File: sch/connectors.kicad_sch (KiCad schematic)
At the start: 79 parts, among them X1 Expansion, X4 PSU

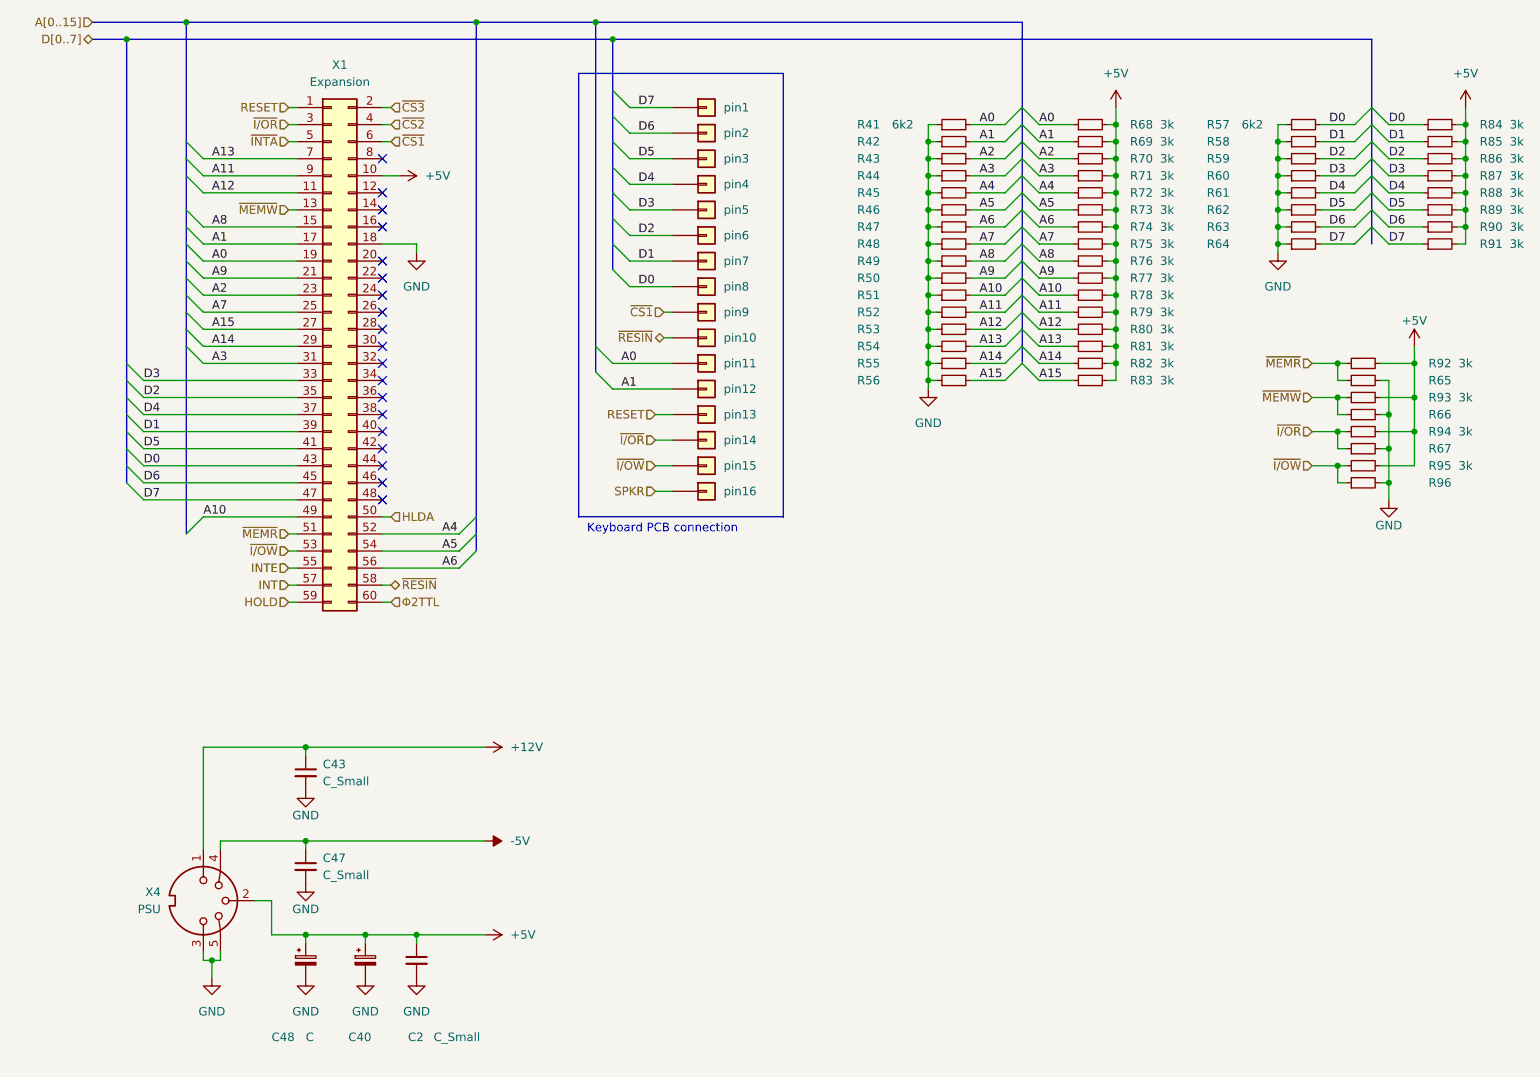
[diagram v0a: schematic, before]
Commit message: Schematics completed with values
Visual corrections pending
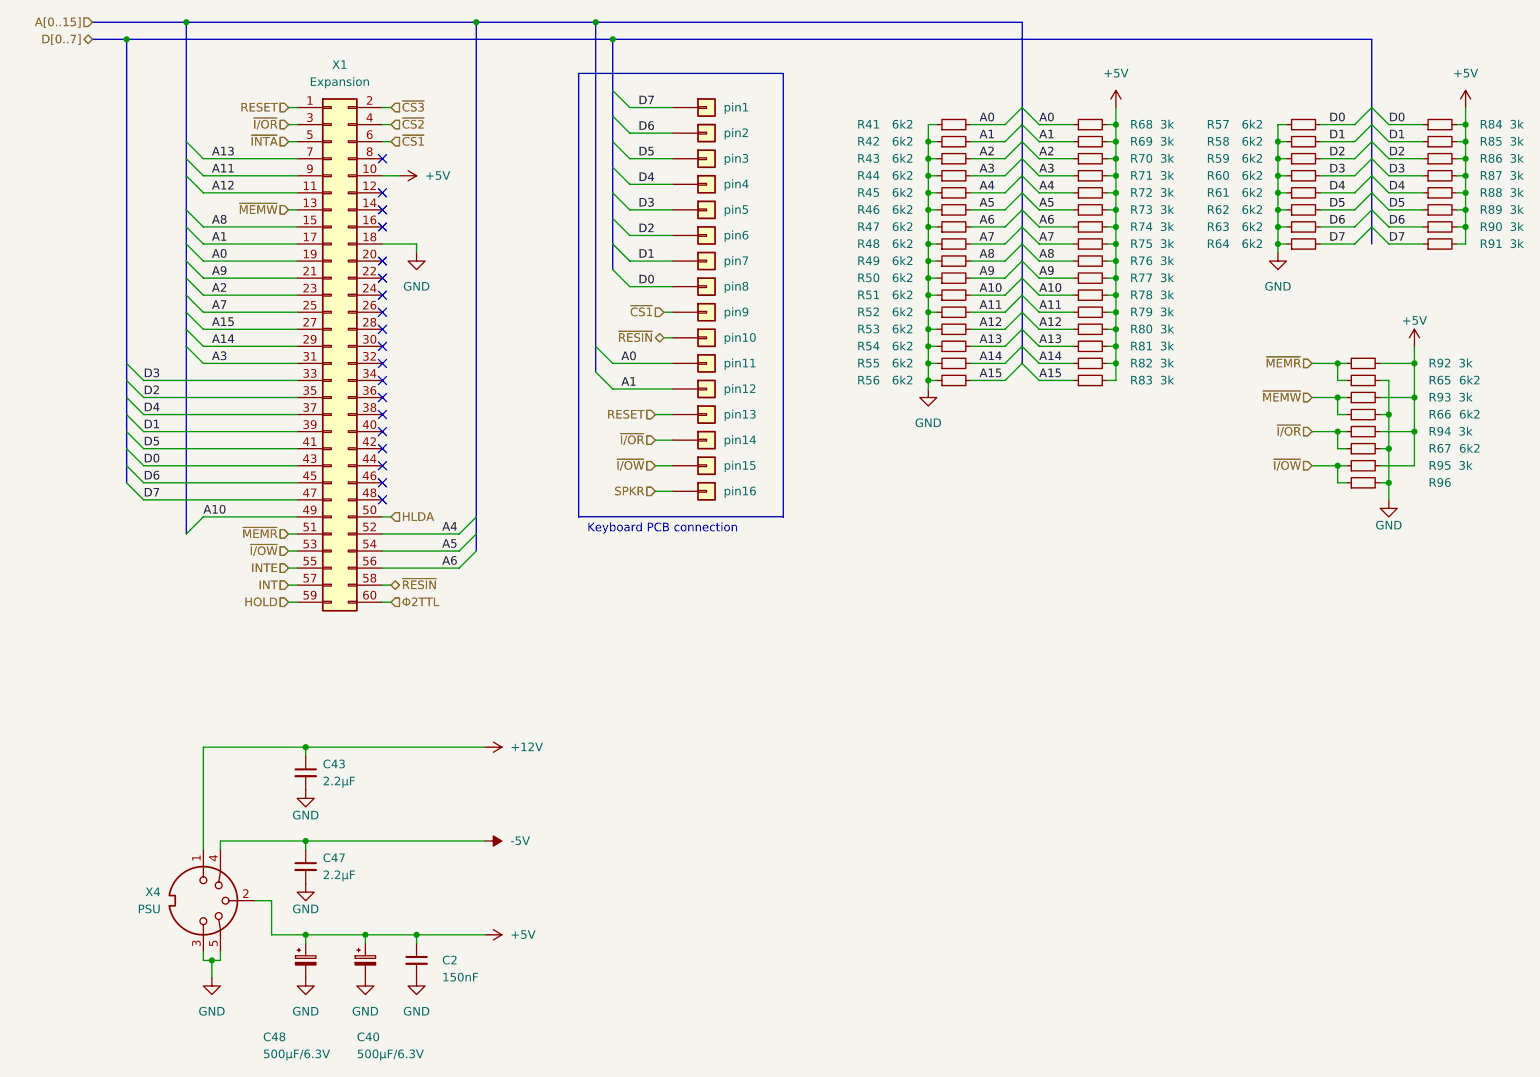
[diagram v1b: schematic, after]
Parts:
- C2: value C_Small -> 150nF
- C40: value ~ -> 500μF/6.3V
- C43, C47: value C_Small -> 2.2μF
- C48: value C -> 500μF/6.3V
- R42, R43, R44, R45, R46, R47, R48, R49, R50, R51, R52, R53, R54, R55, R56, R58, R59, R60, R61, R62, R63, R64, R65, R66, R67: value ~ -> 6k2
- R96: value ~ -> (none)

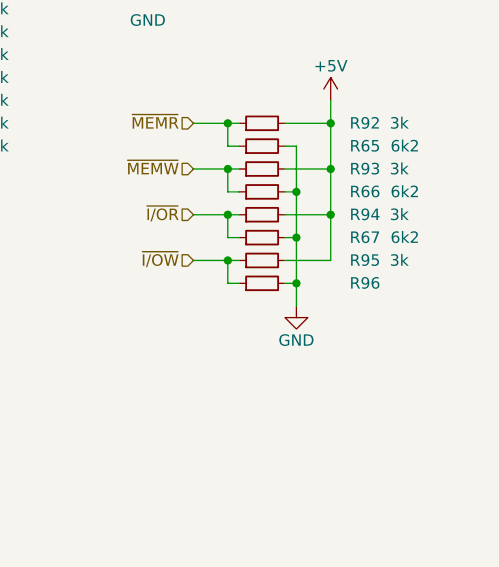
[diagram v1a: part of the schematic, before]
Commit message: Sch: visual corrections
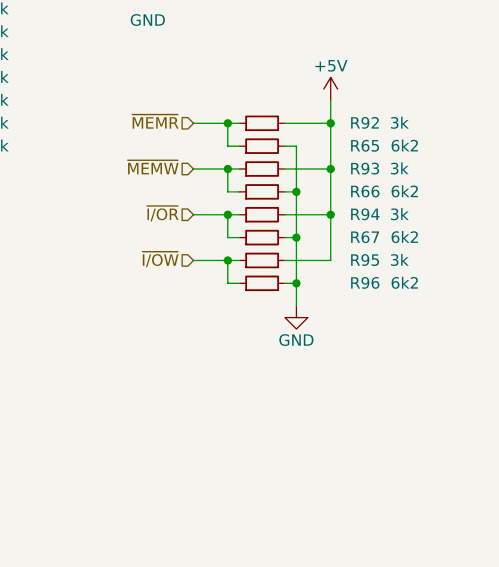
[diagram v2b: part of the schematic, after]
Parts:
- R96: value (none) -> 6k2
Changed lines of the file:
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@@
     (in_bom yes) (on_board yes)
     (property "Reference" "R96" (id 0) (at 245.11 93.98 90))
-    (property "Value" "" (id 1) (at 249.555 93.98 90))
+    (property "Value" "6k2" (id 1) (at 249.555 93.98 90))
     (property "Footprint" "" (id 2) (at 233.68 93.98 0)
       (effects (font (size 1.27 1.27)) hide)
